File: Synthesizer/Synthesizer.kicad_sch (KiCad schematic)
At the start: 0 parts

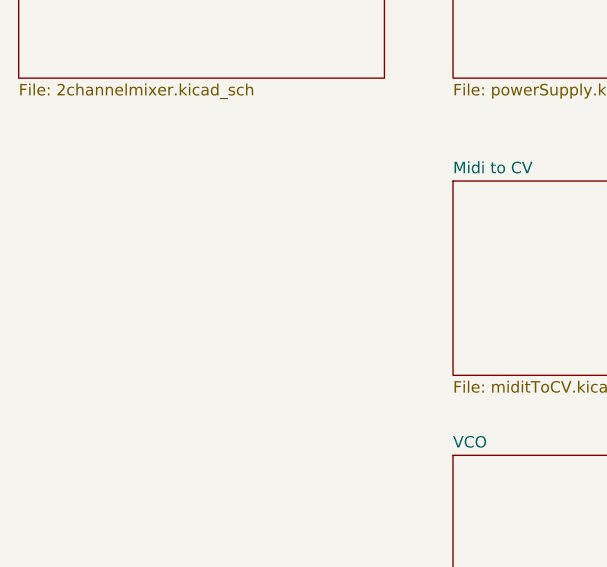
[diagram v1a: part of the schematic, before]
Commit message: Added incomplete VCF and non voltage controlled lpf/hpf
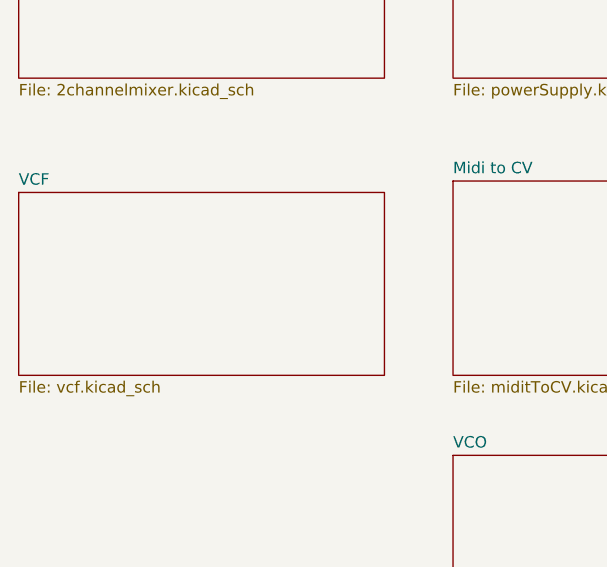
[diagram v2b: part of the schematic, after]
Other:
- added sheet VCF (vcf.kicad_sch)
